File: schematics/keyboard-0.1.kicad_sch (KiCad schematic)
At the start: 1 part, among them U1 nRF52810-QFxx

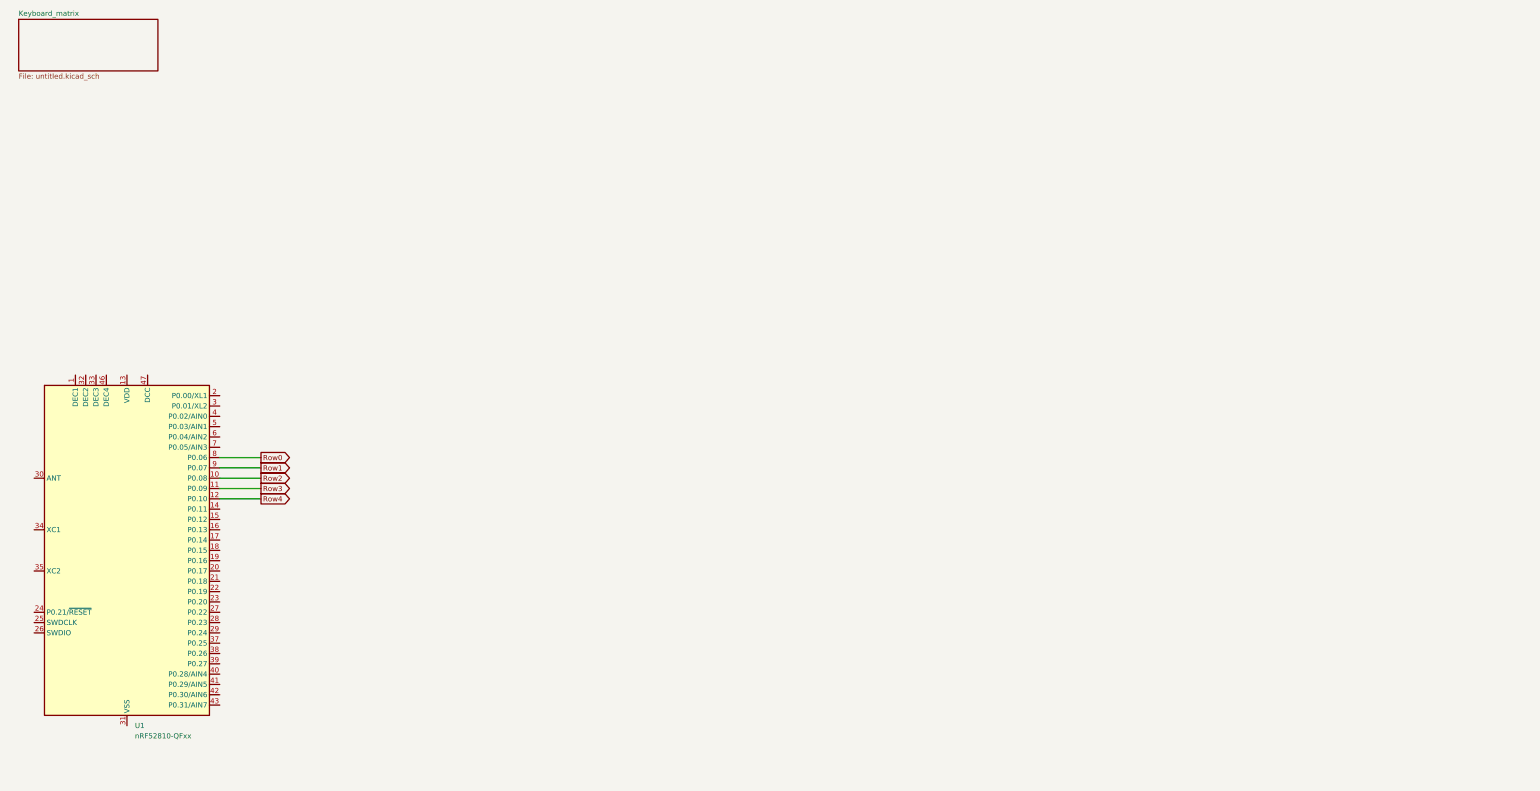
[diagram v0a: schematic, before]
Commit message: (feat) add power flash usb and clock to sch
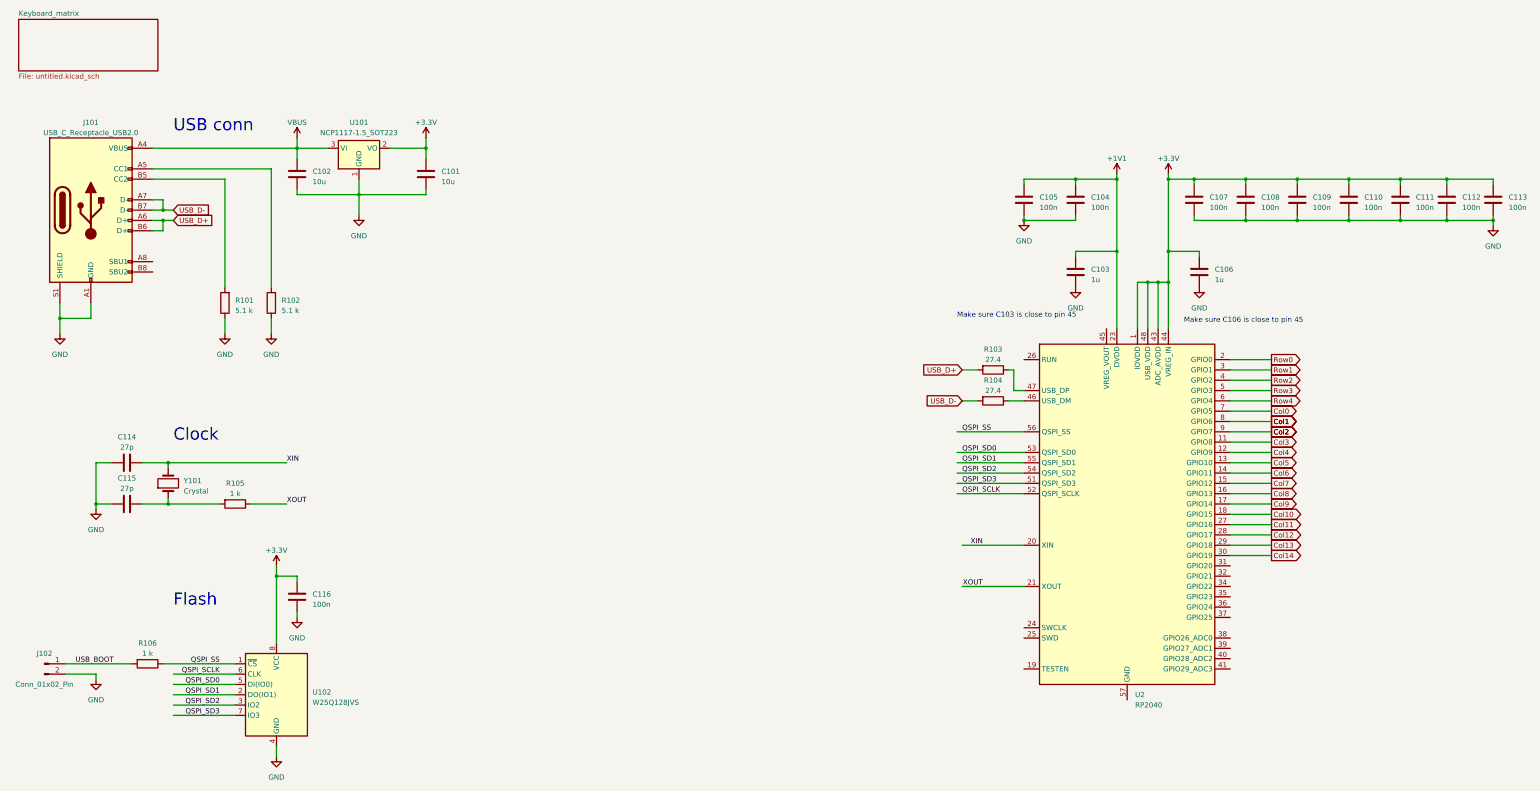
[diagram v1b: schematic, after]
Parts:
- removed U1: nRF52810-QFxx, Package_DFN_QFN:QFN-48-1EP_6x6mm_P0.4mm_EP4.6x4.6mm, symbol MCU_Nordic:nRF52810-QFxx
- added C101, C102: 10u, Capacitor_SMD:C_0201_0603Metric, symbol Device:C
- added C103, C106: 1u, Capacitor_SMD:C_0201_0603Metric, symbol Device:C
- added C104, C105, C107, C108, C109, C110, C111, C112, C113, C116: 100n, Capacitor_SMD:C_0201_0603Metric, symbol Device:C
- added C114, C115: 27p, Capacitor_SMD:C_0201_0603Metric, symbol Device:C
- added J101: USB_C_Receptacle_USB2.0, Connector_USB:USB_C_Receptacle_Amphenol_12401548E4-2A, symbol Connector:USB_C_Receptacle_USB2.0
- added J102: Conn_01x02_Pin, Resistor_SMD:R_0805_2012Metric_Pad1.20x1.40mm_HandSolder, symbol Connector:Conn_01x02_Pin
- added R101, R102: 5.1 k, Resistor_SMD:R_0201_0603Metric, symbol Device:R
- added R103, R104: 27.4, Resistor_SMD:R_0201_0603Metric, symbol Device:R
- added R105, R106: 1 k, Resistor_SMD:R_0201_0603Metric, symbol Device:R
- added U101: NCP1117-1.5_SOT223, Package_TO_SOT_SMD:SOT-223-3_TabPin2, symbol Regulator_Linear:NCP1117-1.5_SOT223
- added U102: W25Q128JVS, Package_SO:SOIC-8_5.23x5.23mm_P1.27mm, symbol Memory_Flash:W25Q128JVS
- added U2: RP2040, Package_DFN_QFN:QFN-56-1EP_7x7mm_P0.4mm_EP3.2x3.2mm, symbol MCU_RaspberryPi:RP2040
- added Y101: Crystal, Crystal:Crystal_SMD_0603-2Pin_6.0x3.5mm, symbol Device:Crystal
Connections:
- net Row0: now also U2.2 (GPIO0)
- net Row1: now also U2.3 (GPIO1)
- net Row2: now also U2.4 (GPIO2)
- net Row3: now also U2.5 (GPIO3)
- net Row4: now also U2.6 (GPIO4)
- new net: C115.2, R105.2, Y101.1
- new net: R104.1, U2.46 (USB_DM)
- new net: R103.1, U2.47 (USB_DP)
- new net: J101.A5 (CC1), R102.2
- new net: J101.B5 (CC2), R101.2
- new net +1V1: C103.1, C104.1, C105.1, U2.23 (DVDD), U2.50 (DVDD)
- new net +3.3V: C101.1, C106.1, C107.1, C108.1, C109.1, C110.1, C111.1, C112.1, C113.1, C116.1, U101.2 (VO), U102.8 (VCC), U2.1 (IOVDD), U2.10 (IOVDD), U2.22 (IOVDD), U2.33 (IOVDD), U2.42 (IOVDD), U2.43 (ADC_AVDD), U2.44 (VREG_IN), U2.48 (USB_VDD), U2.49 (IOVDD)
- new net Col0: U2.7 (GPIO5)
- new net Col1: U2.8 (GPIO6)
- new net Col10: U2.18 (GPIO15)
- new net Col11: U2.27 (GPIO16)
- new net Col12: U2.28 (GPIO17)
- new net Col13: U2.29 (GPIO18)
- new net Col14: U2.30 (GPIO19)
- new net Col2: U2.9 (GPIO7)
- new net Col3: U2.11 (GPIO8)
- new net Col4: U2.12 (GPIO9)
- new net Col5: U2.13 (GPIO10)
- new net Col6: U2.14 (GPIO11)
- new net Col7: U2.15 (GPIO12)
- new net Col8: U2.16 (GPIO13)
- new net Col9: U2.17 (GPIO14)
- new net GND: C101.2, C102.2, C103.2, C104.2, C105.2, C106.2, C107.2, C108.2, C109.2, C110.2, C111.2, C112.2, C113.2, C114.1, C115.1, C116.2, J101.A1 (GND), J101.A12 (GND), J101.B1 (GND), J101.B12 (GND), J101.S1 (SHIELD), J102.2 (Pin_2), R101.1, R102.1, U101.1 (GND), U102.4 (GND)
- new net QSPI_SCLK: U102.6 (CLK), U2.52 (QSPI_SCLK)
- new net QSPI_SD0: U102.5 (DI(IO0)), U2.53 (QSPI_SD0)
- new net QSPI_SD1: U102.2 (DO(IO1)), U2.55 (QSPI_SD1)
- new net QSPI_SD2: U102.3 (IO2), U2.54 (QSPI_SD2)
- new net QSPI_SD3: U102.7 (IO3), U2.51 (QSPI_SD3)
- new net QSPI_SS: R106.1, U102.1 (~{CS}), U2.56 (QSPI_SS)
- new net USB_BOOT: J102.1 (Pin_1), R106.2
- new net USB_D+: J101.A6 (D+), J101.B6 (D+), R103.2
- new net USB_D-: J101.A7 (D-), J101.B7 (D-), R104.2
- new net VBUS: C102.1, J101.A4 (VBUS), J101.A9 (VBUS), J101.B4 (VBUS), J101.B9 (VBUS), U101.3 (VI)
- new net XIN: C114.2, U2.20 (XIN), Y101.2
- new net XOUT: R105.1, U2.21 (XOUT)
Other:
- note added: "Clock"
- note added: "Flash"
- note added: "Make sure C103 is close to pin 45"
- note added: "Make sure C106 is close to pin 45"
- note added: "USB conn"
